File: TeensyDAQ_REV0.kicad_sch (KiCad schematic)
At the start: 0 parts

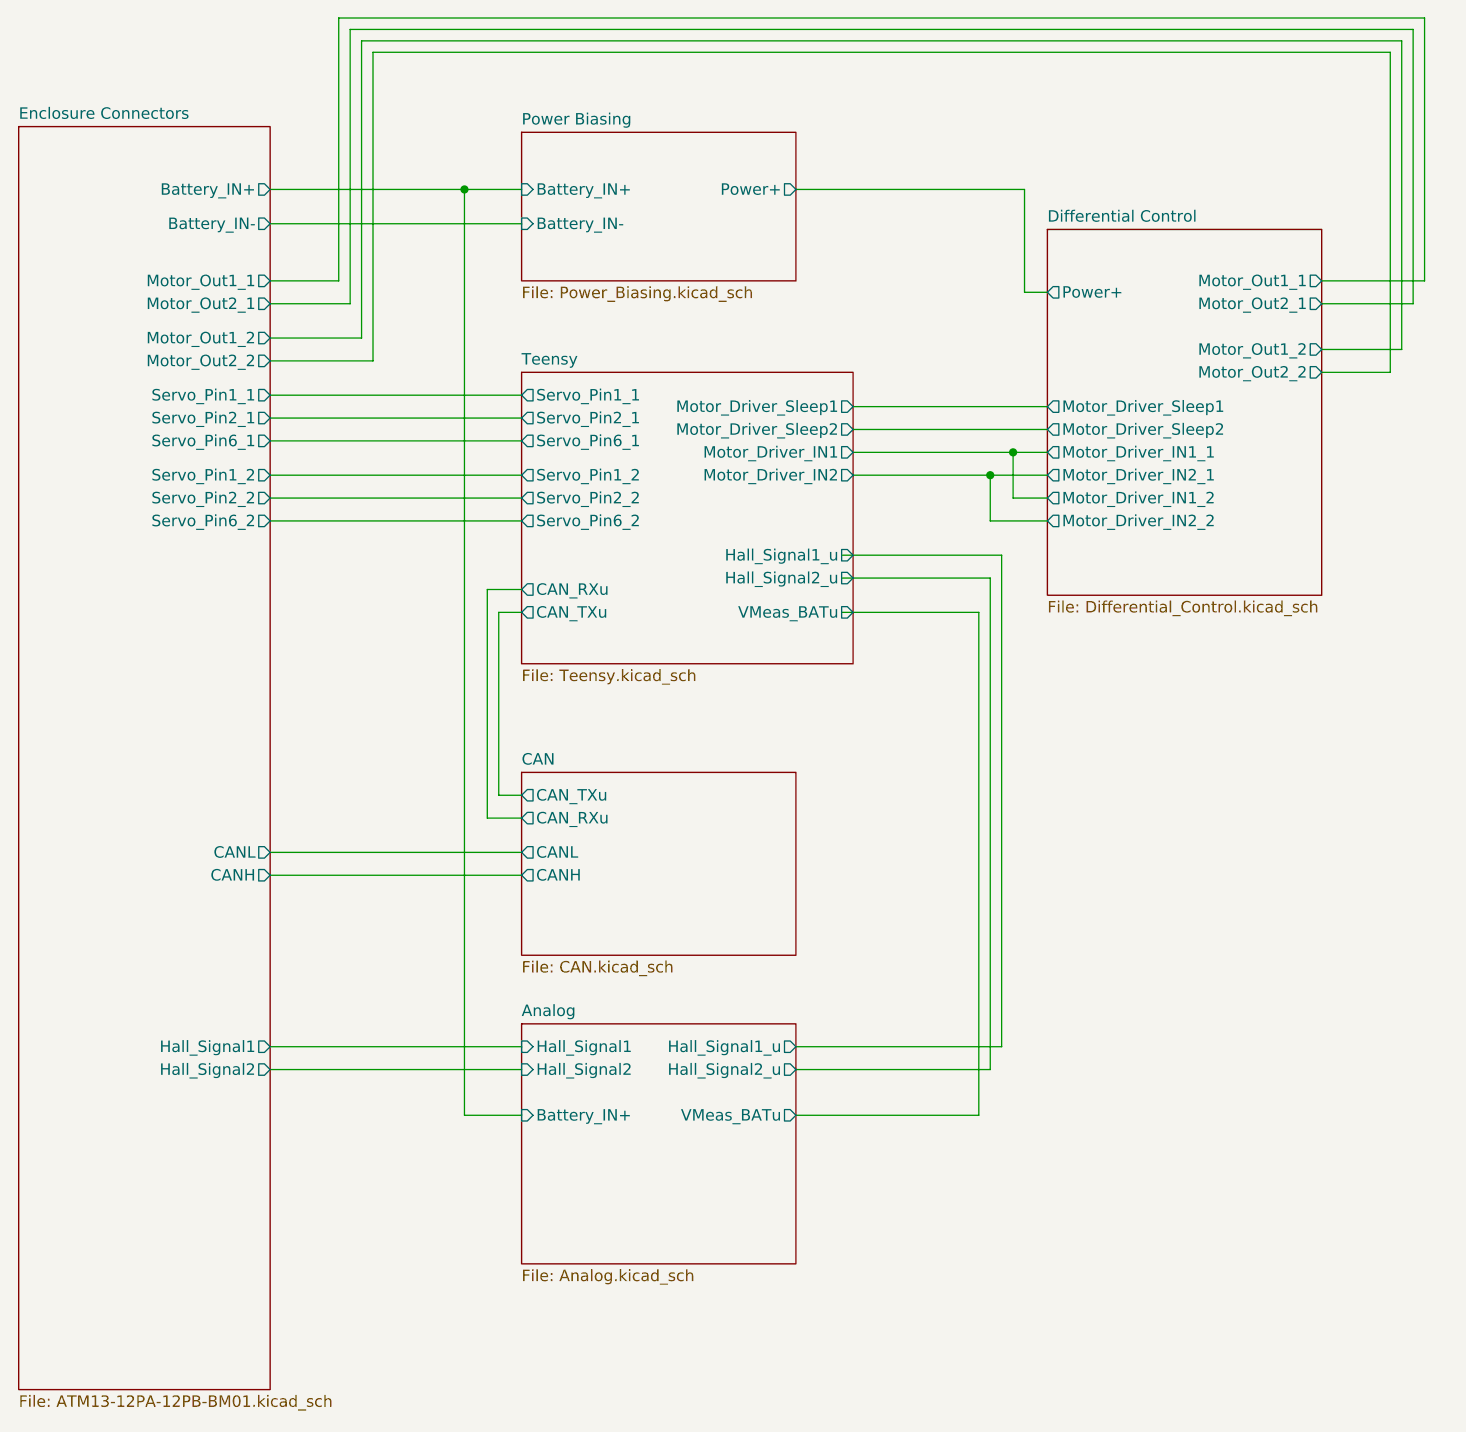
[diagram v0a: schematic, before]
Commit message: Added gyro, current sense, removed servo control, added temp sense
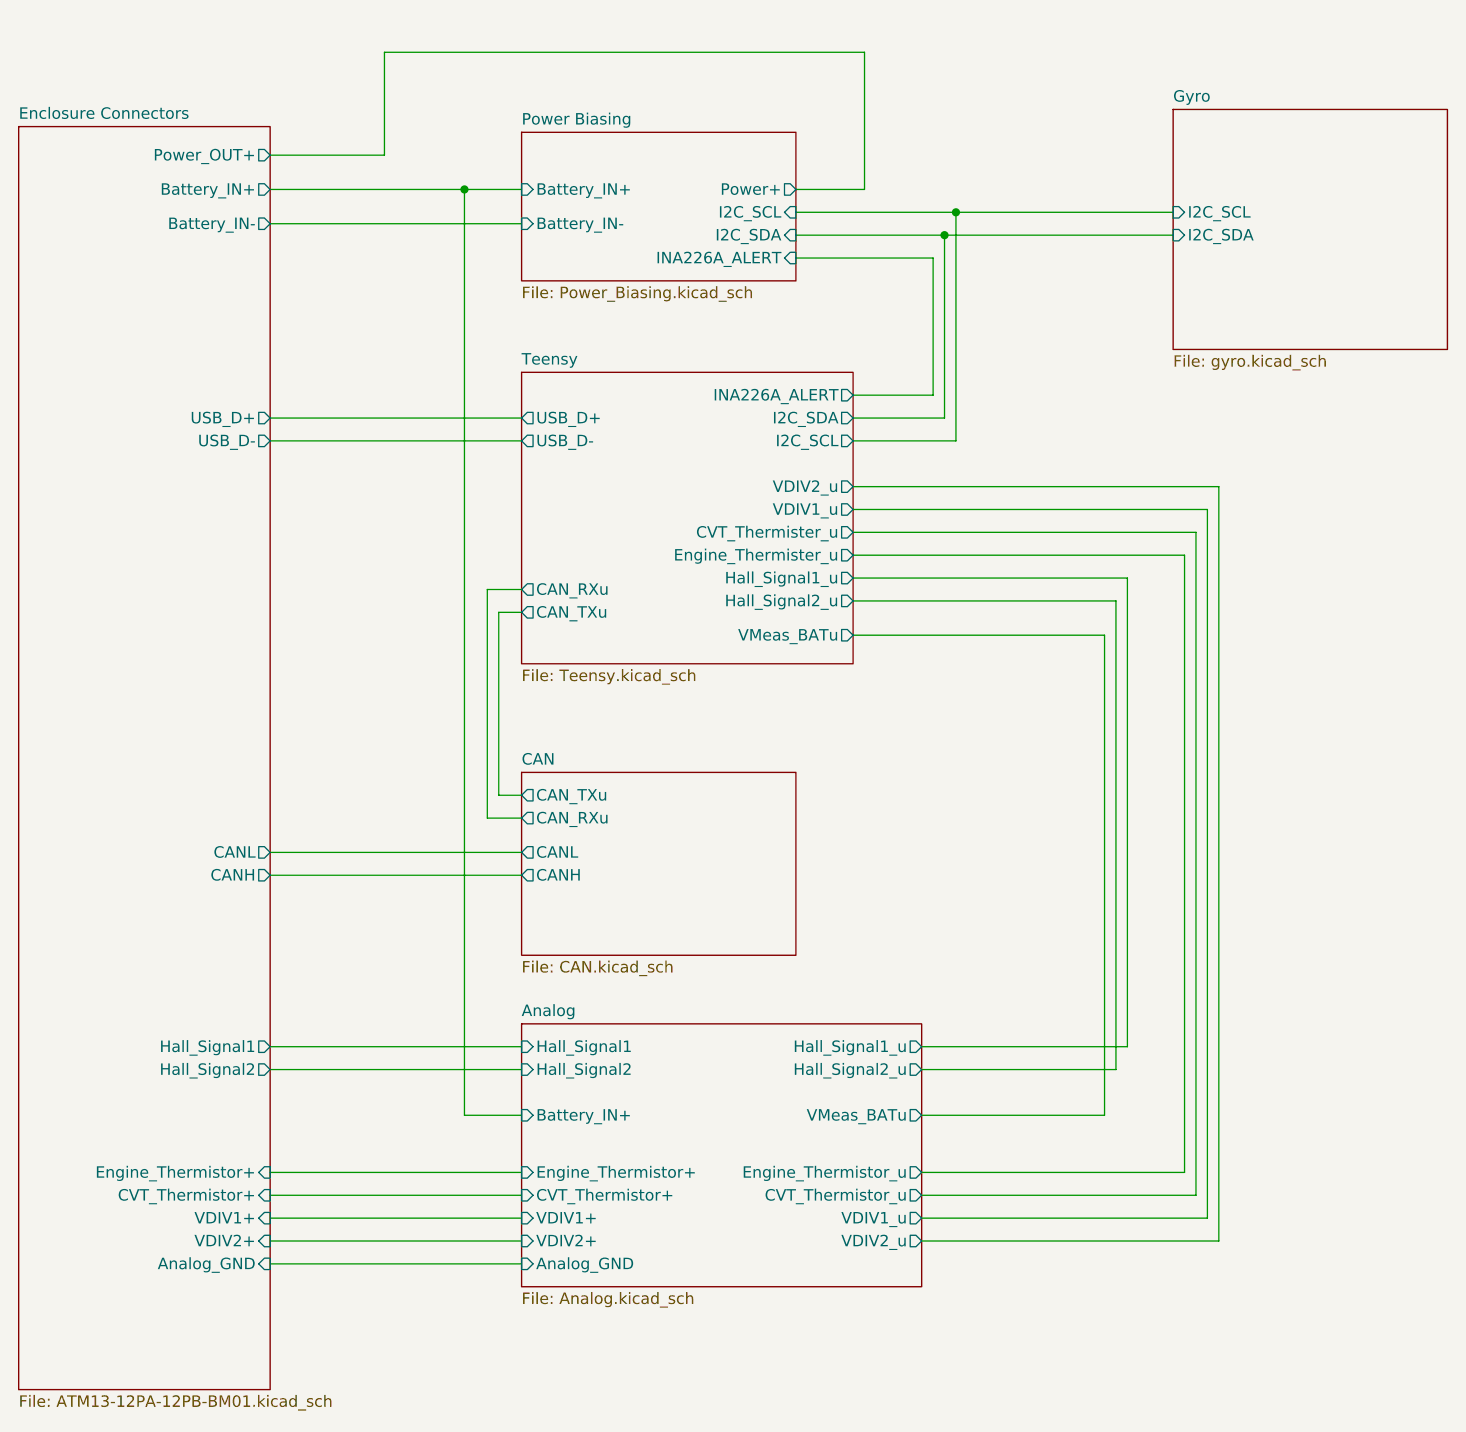
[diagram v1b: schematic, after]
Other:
- removed sheet Differential Control
- added sheet Gyro (gyro.kicad_sch)
- sheet Analog ports: added Analog_GND, CVT_Thermistor+, CVT_Thermistor_u, Engine_Thermistor+, Engine_Thermistor_u, VDIV1+, VDIV1_u, VDIV2+, VDIV2_u; removed none
- sheet Enclosure Connectors ports: added Analog_GND, CVT_Thermistor+, Engine_Thermistor+, Power_OUT+, USB_D+, USB_D-, VDIV1+, VDIV2+; removed Motor_Out1_1, Motor_Out1_2, Motor_Out2_1, Motor_Out2_2, Servo_Pin1_1, Servo_Pin1_2, Servo_Pin2_1, Servo_Pin2_2, Servo_Pin6_1, Servo_Pin6_2
- sheet Power Biasing ports: added I2C_SCL, I2C_SDA, INA226A_ALERT; removed none
- sheet Teensy ports: added CVT_Thermister_u, Engine_Thermister_u, I2C_SCL, I2C_SDA, INA226A_ALERT, USB_D+, USB_D-, VDIV1_u, VDIV2_u; removed Motor_Driver_IN1, Motor_Driver_IN2, Motor_Driver_Sleep1, Motor_Driver_Sleep2, Servo_Pin1_1, Servo_Pin1_2, Servo_Pin2_1, Servo_Pin2_2, Servo_Pin6_1, Servo_Pin6_2

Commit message: finished up schematic, added magnetic sensor, cleaned up pins, etc.
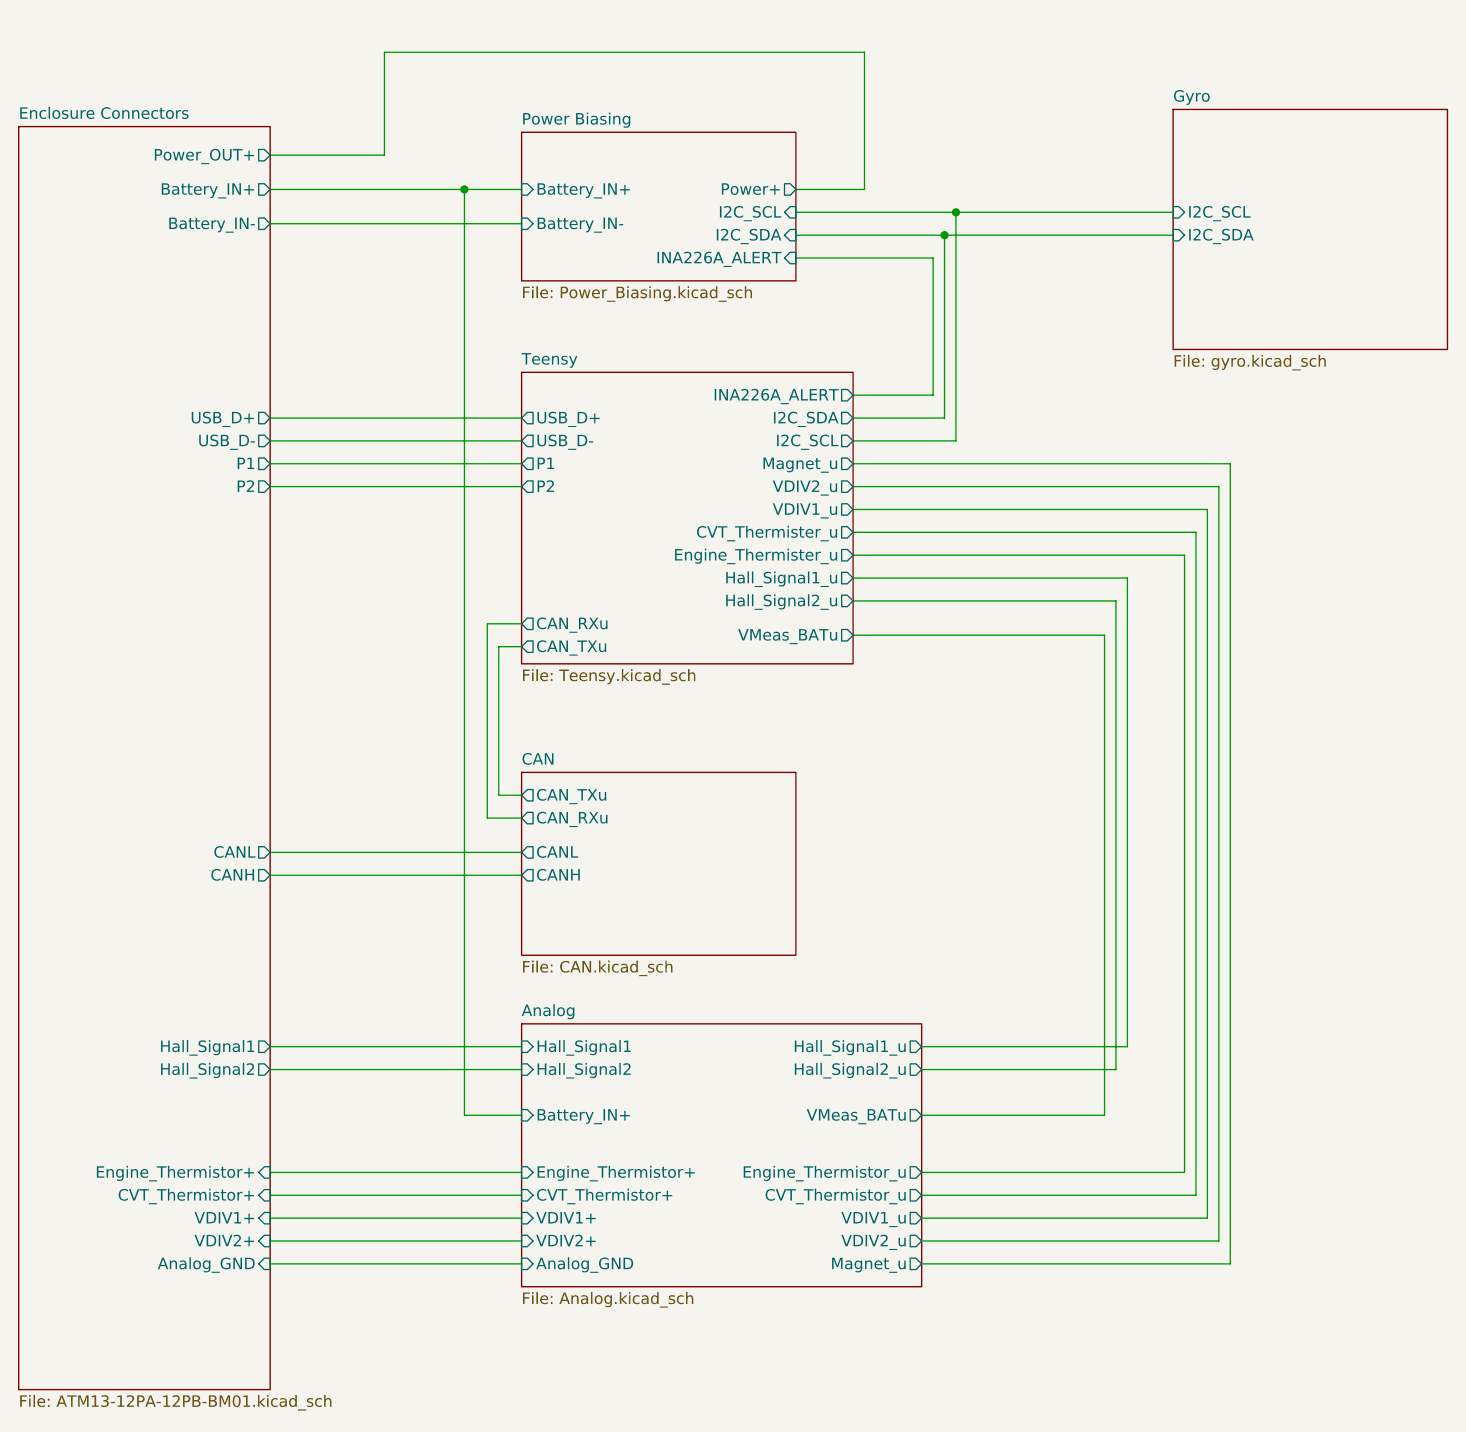
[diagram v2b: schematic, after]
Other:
- sheet Analog ports: added Magnet_u; removed none
- sheet Enclosure Connectors ports: added P1, P2; removed none
- sheet Teensy ports: added Magnet_u, P1, P2; removed none
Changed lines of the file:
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@@
+	(wire
+		(pts
+			(xy 124.46 72.39) (xy 166.37 72.39)
+		)
+		(stroke
+			(width 0)
+			(type default)
+		)
+	)
 	(wire
 		(pts
@@
 	(wire
 		(pts
+			(xy 166.37 72.39) (xy 166.37 161.29)
+		)
+		(stroke
+			(width 0)
+			(type default)
+		)
+	)
+	(wire
+		(pts
 			(xy 59.69 69.85) (xy 87.63 69.85)
 		)
@@
 	(wire
 		(pts
-			(xy 87.63 86.36) (xy 83.82 86.36)
+			(xy 87.63 90.17) (xy 83.82 90.17)
 		)
 		(stroke
@@
 	(wire
 		(pts
+			(xy 59.69 74.93) (xy 87.63 74.93)
+		)
+		(stroke
+			(width 0)
+			(type default)
+		)
+	)
+	(wire
+		(pts
 			(xy 124.46 69.85) (xy 135.89 69.85)
 		)
@@
 	(wire
 		(pts
+			(xy 166.37 161.29) (xy 132.08 161.29)
+		)
+		(stroke
+			(width 0)
+			(type default)
+		)
+	)
+	(wire
+		(pts
 			(xy 59.69 45.72) (xy 87.63 45.72)
 		)
@@
 	(wire
 		(pts
-			(xy 83.82 86.36) (xy 83.82 111.76)
+			(xy 83.82 90.17) (xy 83.82 111.76)
 		)
 		(stroke
@@
 	(wire
 		(pts
-			(xy 85.09 88.9) (xy 85.09 109.22)
+			(xy 85.09 92.71) (xy 85.09 109.22)
 		)
 		(stroke
@@
 	(wire
 		(pts
+			(xy 59.69 72.39) (xy 87.63 72.39)
+		)
+		(stroke
+			(width 0)
+			(type default)
+		)
+	)
+	(wire
+		(pts
 			(xy 124.46 87.63) (xy 153.67 87.63)
 		)
@@
 	(wire
 		(pts
-			(xy 87.63 88.9) (xy 85.09 88.9)
+			(xy 87.63 92.71) (xy 85.09 92.71)
 		)
 		(stroke
@@
 			)
 		)
+		(pin "P2" output
+			(at 59.69 74.93 0)
+			(effects
+				(font
+					(size 1.27 1.27)
+				)
+				(justify right)
+			)
+		)
+		(pin "P1" output
+			(at 59.69 72.39 0)
+			(effects
+				(font
+					(size 1.27 1.27)
+				)
+				(justify right)
+			)
+		)
 		(instances
 			(project "TeensyDAQ_REV0"
@@
 		)
 		(pin "CAN_RXu" output
-			(at 87.63 86.36 180)
+			(at 87.63 90.17 180)
 			(effects
 				(font
@@
 		)
 		(pin "CAN_TXu" output
-			(at 87.63 88.9 180)
+			(at 87.63 92.71 180)
 			(effects
 				(font
@@
 				)
 				(justify right)
+			)
+		)
+		(pin "P1" output
+			(at 87.63 72.39 180)
+			(effects
+				(font
+					(size 1.27 1.27)
+				)
+				(justify left)
+			)
+		)
+		(pin "Magnet_u" output
+			(at 124.46 72.39 0)
+			(effects
+				(font
+					(size 1.27 1.27)
+				)
+				(justify right)
+			)
+		)
+		(pin "P2" output
+			(at 87.63 74.93 180)
+			(effects
+				(font
+					(size 1.27 1.27)
+				)
+				(justify left)
 			)
 		)
@@
 			(effects
 				(font
+					(size 1.27 1.27)
+				)
+				(justify right)
+			)
+		)
+		(pin "Magnet_u" output
+			(at 132.08 161.29 0)
+			(effects
+				(font

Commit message: removed a VDIV input and changed it to a thermistor input. Re-ran fabrication output
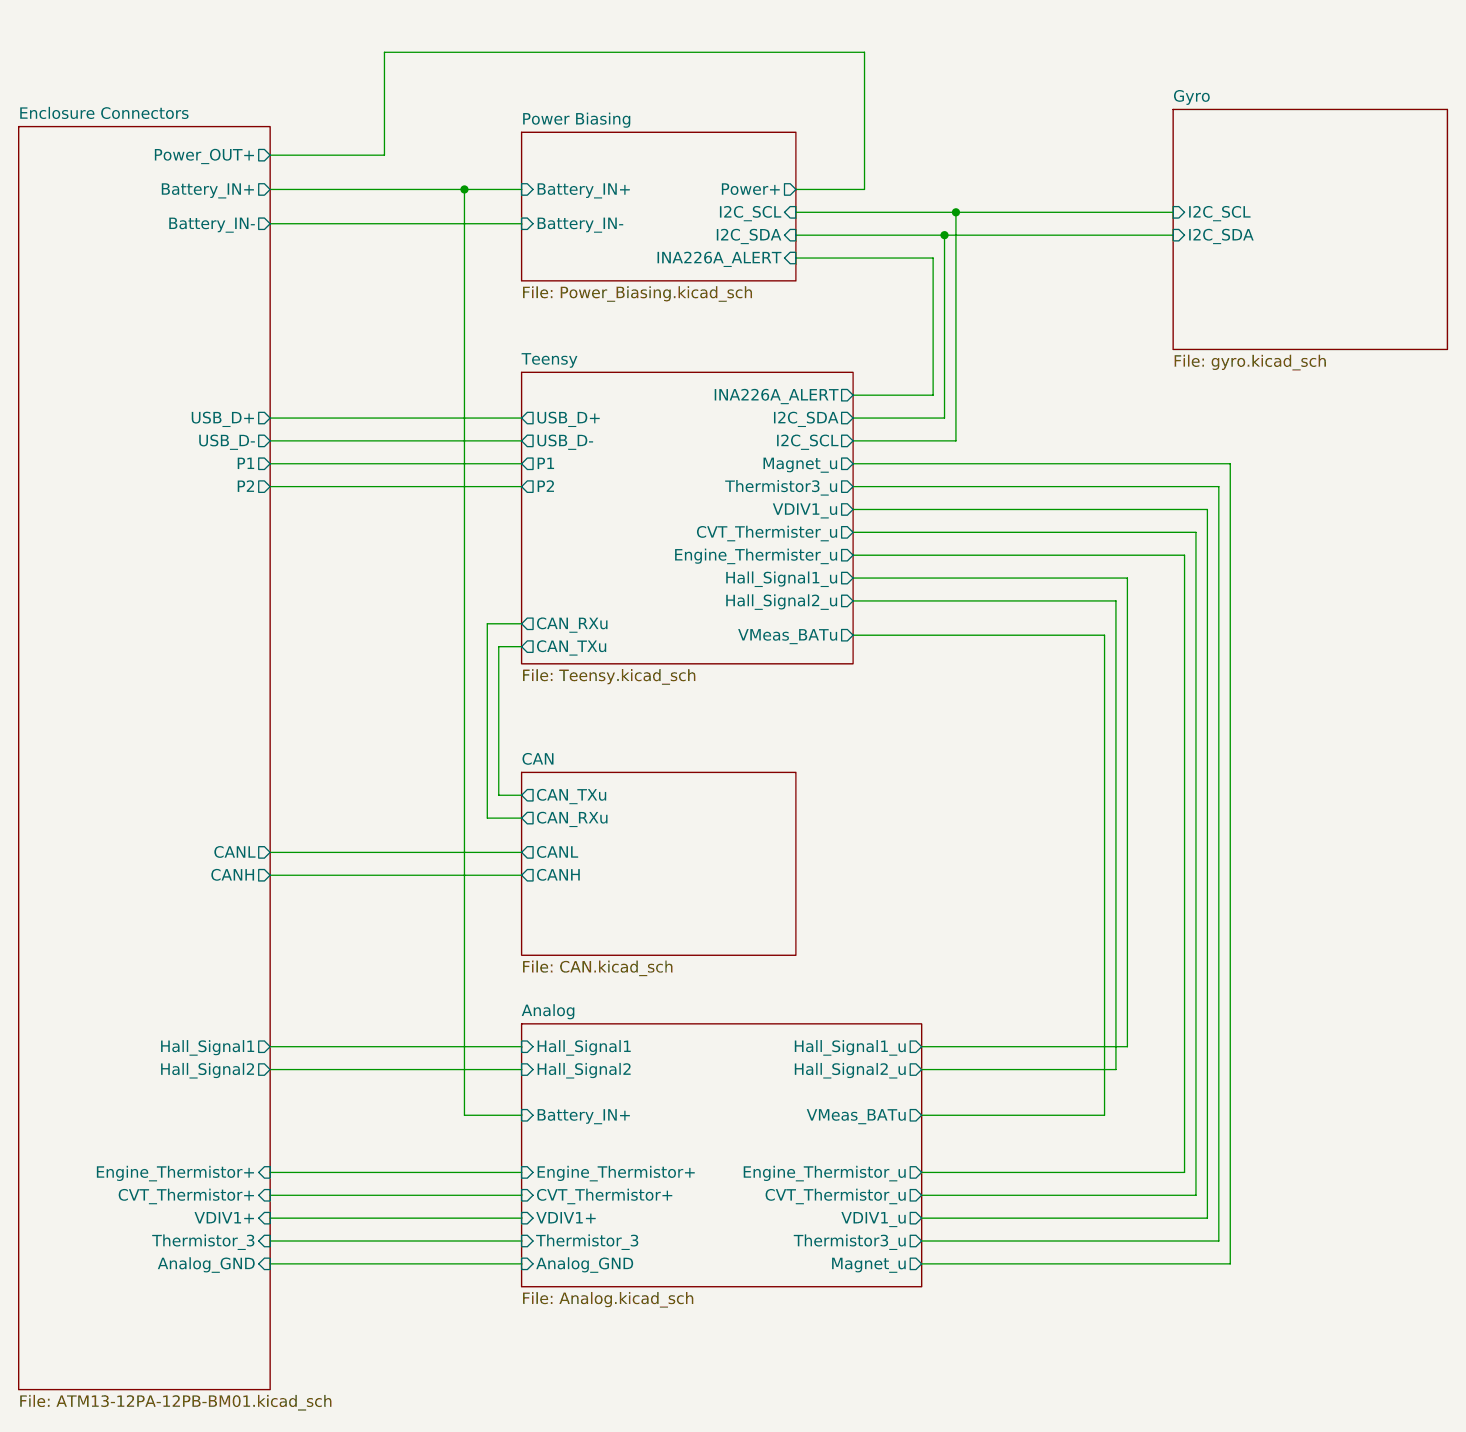
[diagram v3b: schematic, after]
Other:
- sheet Analog ports: added Thermistor3_u, Thermistor_3; removed VDIV2+, VDIV2_u
- sheet Enclosure Connectors ports: added Thermistor_3; removed VDIV2+
- sheet Teensy ports: added Thermistor3_u; removed VDIV2_u
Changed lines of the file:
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@@
-			)
-		)
-		(pin "VDIV2+" input
-			(at 59.69 158.75 0)
-			(effects
-				(font
-					(size 1.27 1.27)
-				)
-				(justify right)
 			)
 		)
@@
 		(pin "P1" output
 			(at 59.69 72.39 0)
+			(effects
+				(font
+					(size 1.27 1.27)
+				)
+				(justify right)
+			)
+		)
+		(pin "Thermistor_3" input
+			(at 59.69 158.75 0)
 			(effects
 				(font
@@
 			)
 		)
-		(pin "VDIV2_u" output
-			(at 124.46 74.93 0)
-			(effects
-				(font
-					(size 1.27 1.27)
-				)
-				(justify right)
-			)
-		)
 		(pin "I2C_SDA" output
 			(at 124.46 67.31 0)
@@
 				)
 				(justify left)
+			)
+		)
+		(pin "Thermistor3_u" output
+			(at 124.46 74.93 0)
+			(effects
+				(font
+					(size 1.27 1.27)
+				)
+				(justify right)
 			)
 		)
@@
 			)
 		)
-		(pin "VDIV2+" input
-			(at 87.63 158.75 180)
-			(effects
-				(font
-					(size 1.27 1.27)
-				)
-				(justify left)
-			)
-		)
-		(pin "VDIV2_u" output
-			(at 132.08 158.75 0)
-			(effects
-				(font
-					(size 1.27 1.27)
-				)
-				(justify right)
-			)
-		)
 		(pin "Magnet_u" output
 			(at 132.08 161.29 0)
@@
 			)
 		)
+		(pin "Thermistor3_u" output
+			(at 132.08 158.75 0)
+			(effects
+				(font
+					(size 1.27 1.27)
+				)
+				(justify right)
+			)
+		)
+		(pin "Thermistor_3" input
+			(at 87.63 158.75 180)
+			(effects
+				(font
+					(size 1.27 1.27)
+				)
+				(justify left)
+			)
+		)
